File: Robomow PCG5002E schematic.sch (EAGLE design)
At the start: 10 parts, among them J1 RJ11-2L-B

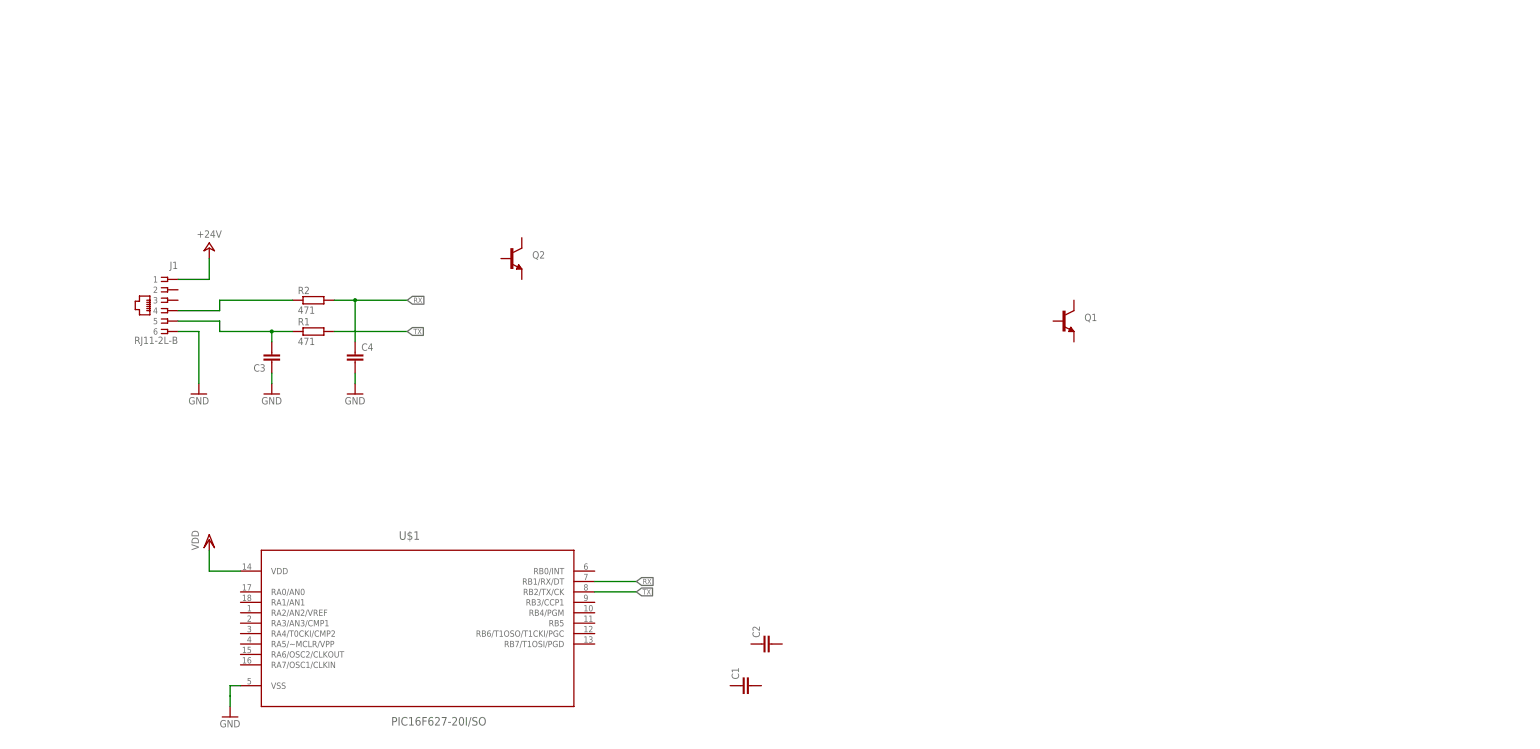
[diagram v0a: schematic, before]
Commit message: Added perimeter schematic
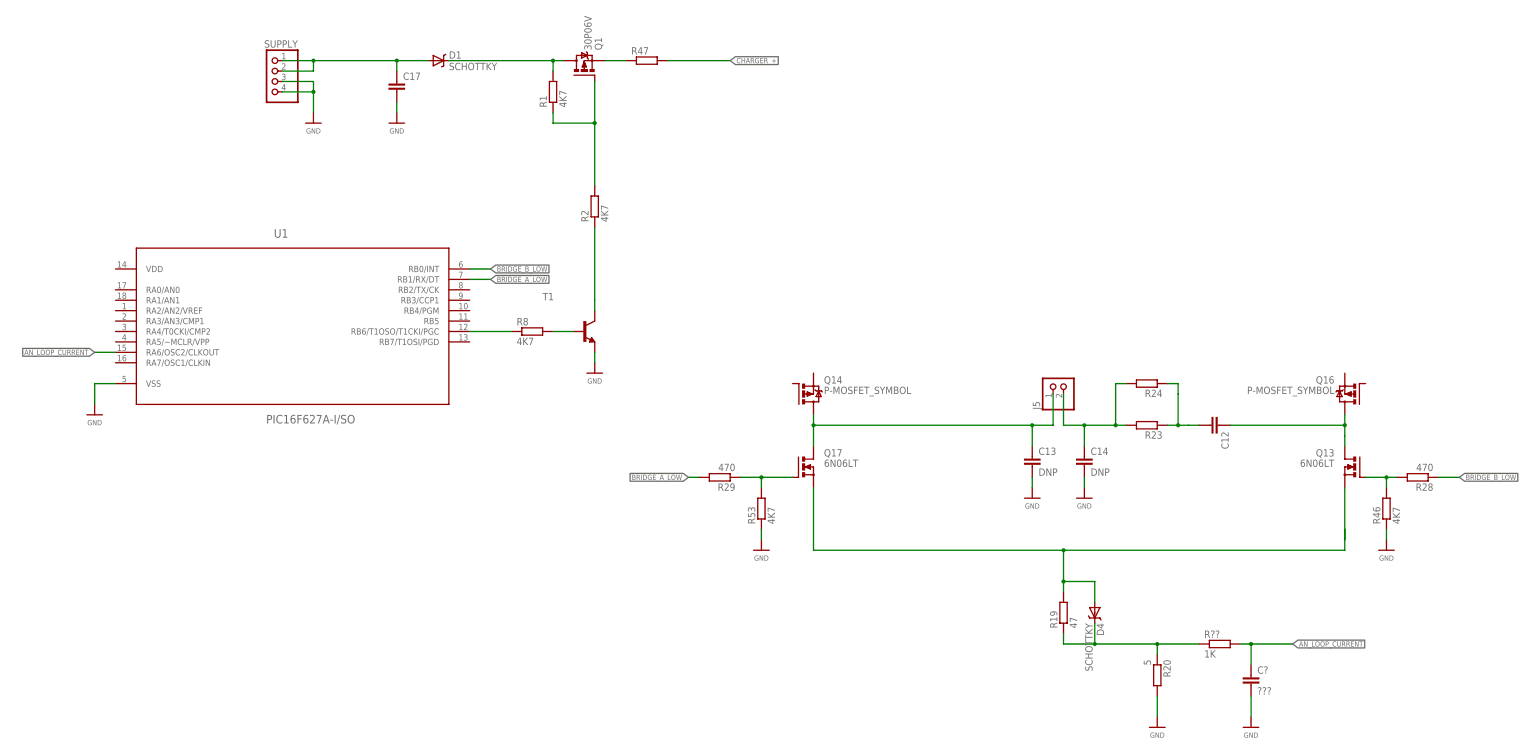
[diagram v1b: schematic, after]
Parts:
- removed C1, C2, C3, C4: (no value), rcl:C-EUC0805
- removed J1: RJ11-2L-B, con-tycoelectronics:RJ11-2L-B
- removed Q1, Q2: (no value), SparkFun:TRANSISTOR_NPNSOT89
- removed U$1: PIC16F627-20I/SO, Microchip_By_element14_Batch_1:PIC16F627-20I/SO
- added C12, C17: (no value), rcl:C-EU050-030X075
- added C13, C14: DNP, rcl:C-EUC0603
- added C?: ???, rcl:C-EUC0603
- added D1, D4: SCHOTTKY, Ava2:SCHOTTKY
- added J5: (no value), pinhead:PINHD-1X2
- added R19: 47, rcl:R-EU_R0603
- added R20: 5, rcl:R-EU_R0603
- added R23, R24, R47: (no value), rcl:R-EU_0414/15
- added R28, R29: 470, rcl:R-EU_R0603
- added R46, R53, R8: 4K7, rcl:R-EU_R0603
- added R??: 1K, rcl:R-EU_R0603
- added SUPPLY: (no value), pinhead:PINHD-1X4
- added T1: (no value), transistor:-NPN-SOT23-EBC
- added U1: PIC16F627A-I/SO, Microchip_By_element14_Batch_1:PIC16F627A-I/SO
- R1, R2: value 471 -> 4K7; device rcl:R-EU_R0805 -> rcl:R-EU_R0603
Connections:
- removed net +24V: J1.1
- removed net RX: C4.1, R2.2, U$1.RB1/RX/DT
- removed net RX_R: J1.4, R2.1
- removed net TX: R1.2, U$1.RB2/TX/CK
- removed net TX_R: C3.2, J1.5, R1.1
- removed net VDD: U$1.VDD
- new net AN_LOOP_CURRENT: C?.1, R??.2, U1.RA6/OSC2/CLKOUT
- new net BRIDGE_A_LOW: R29.2, U1.RB1/RX/DT
- new net BRIDGE_B_LOW: R28.1, U1.RB0/INT
- new net CHARGER_+: R47.2
- new net N$1: R8.1, U1.RB6/T1OSO/T1CKI/PGC
- new net N$10: C13.1, J5.1
- new net N$11: C12.2, R23.1, R24.1
- new net N$12: R28.2, R46.2
- new net N$13: D4.A, R19.2
- new net N$14: C14.1, J5.2, R23.2, R24.2
- new net N$15: C12.1
- new net N$16: D4.C, R19.1, R20.1, R??.1
- new net N$2: R8.2, T1.B
- new net N$3: D1.C, R1.2
- new net N$4: R1.1, R2.2
- new net N$5: C17.1, D1.A, SUPPLY.1, SUPPLY.2
- new net N$6: R2.1, T1.C
- new net N$7: R47.1
- new net N$8: R29.1, R53.2
- net GND: now also C13.2, C14.2, C17.2, C?.2, R20.2, R46.1, R53.1, SUPPLY.3, SUPPLY.4, T1.E, U1.VSS; no longer C3.1, C4.2, J1.6, U$1.VSS
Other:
- moved on the sheet: R1, R2
